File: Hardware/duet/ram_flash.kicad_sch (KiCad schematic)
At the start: 1 part, among them U2 W956D8MBYA5I

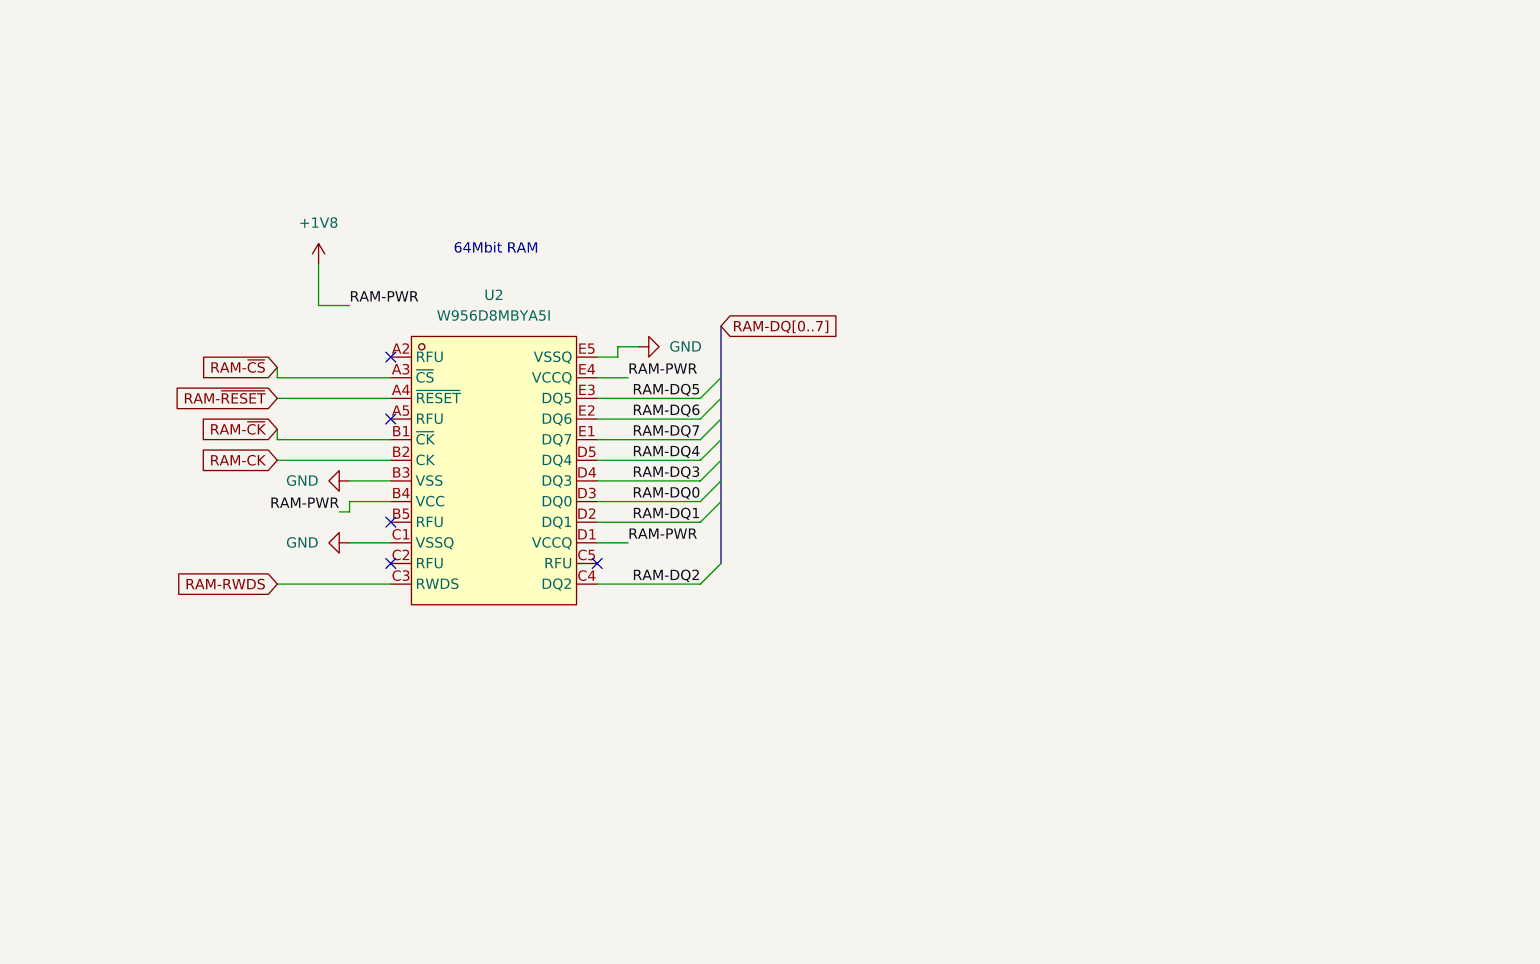
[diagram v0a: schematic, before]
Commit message: Add ECP5 configuration pins and labels
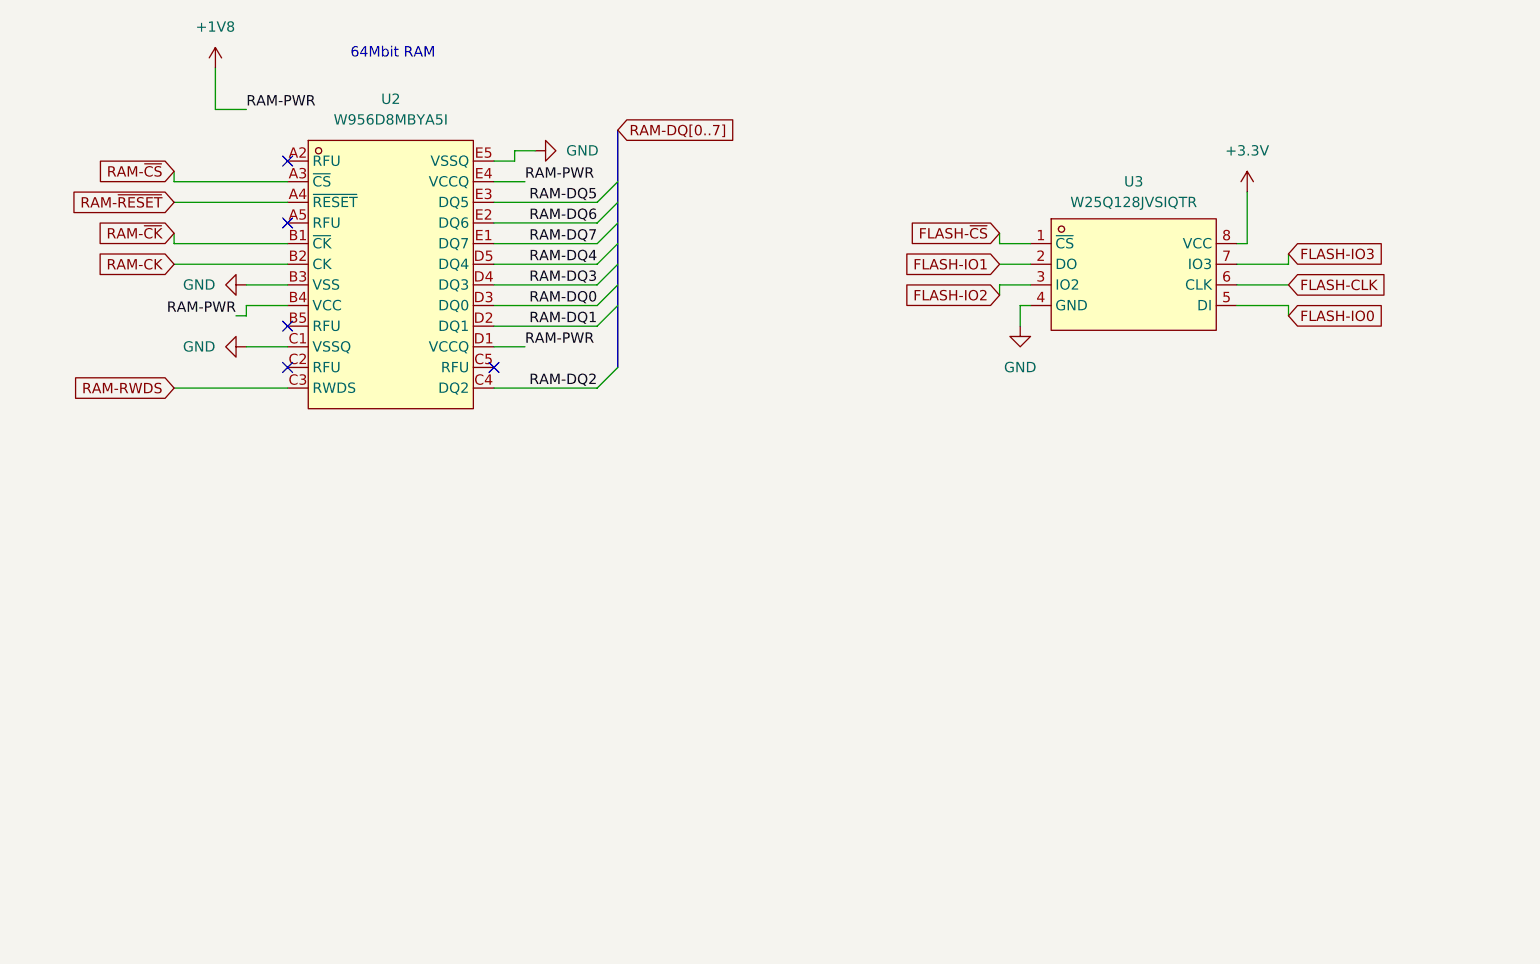
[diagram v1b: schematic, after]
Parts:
- added U3: W25Q128JVSIQTR, easyeda2kicad:SOIC-8_L5.3-W5.3-P1.27-LS8.0-BL, symbol easyeda2kicad:W25Q128JVSIQTR
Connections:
- net GND: now also U3.4 (GND)
- new net +3.3V: U3.8 (VCC)
- new net FLASH-CLK: U3.6 (CLK)
- new net FLASH-IO0: U3.5 (DI)
- new net FLASH-IO1: U3.2 (DO)
- new net FLASH-IO2: U3.3 (IO2)
- new net FLASH-IO3: U3.7 (IO3)
- new net FLASH-~{CS}: U3.1 (~{CS})
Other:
- moved on the sheet: U2

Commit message: Adds HDMI transmitter and connector
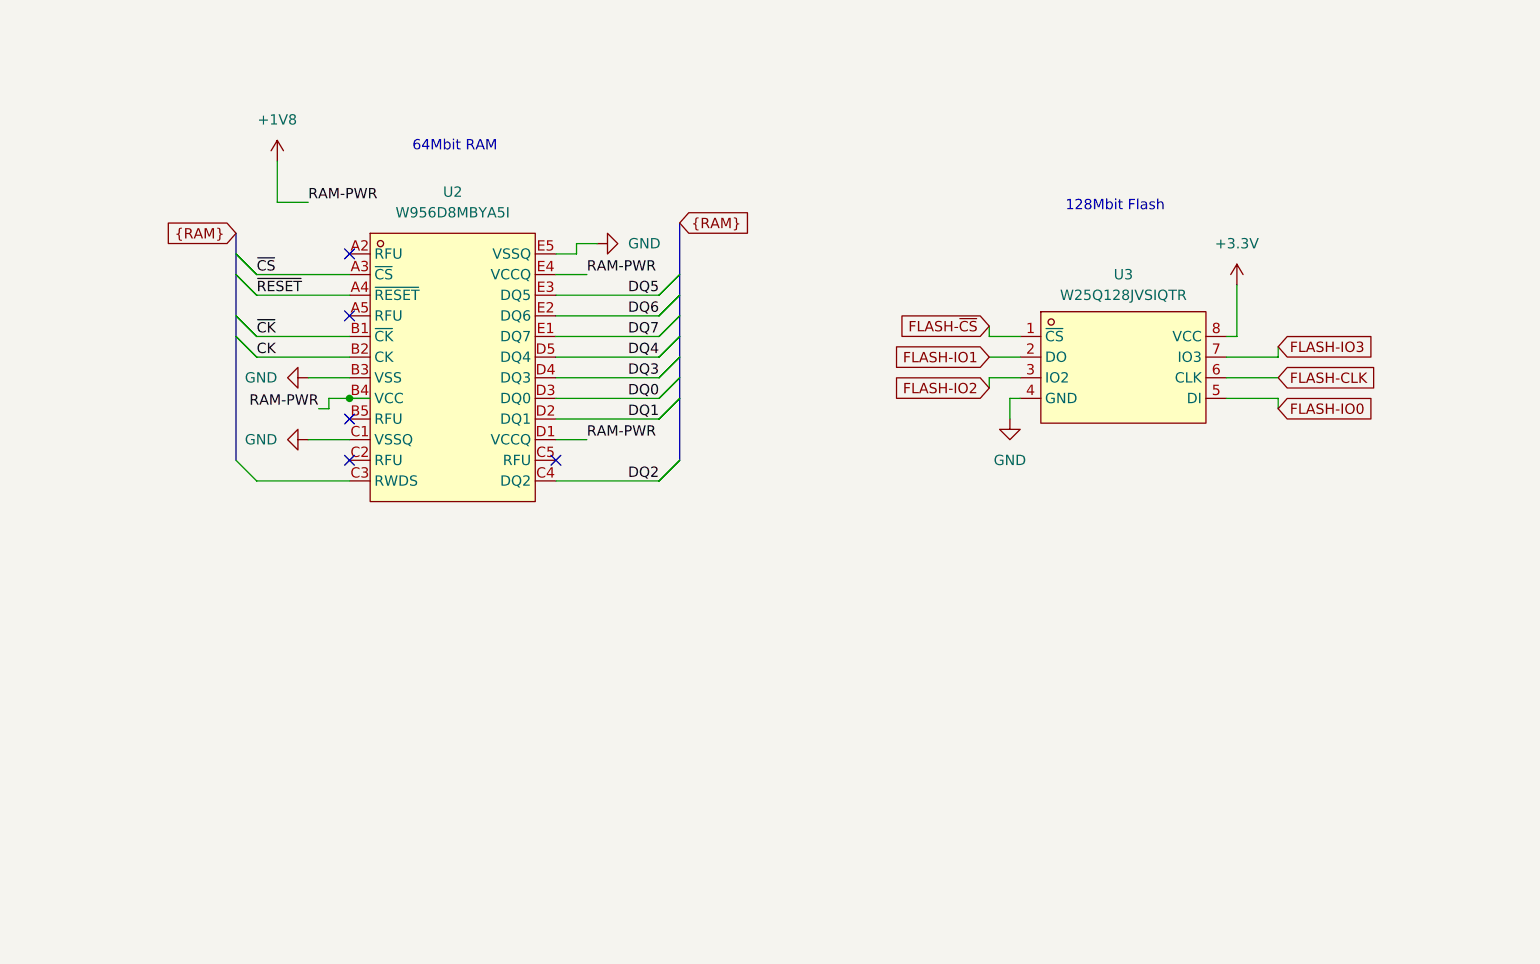
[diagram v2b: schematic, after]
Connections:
- net RAM-CK renamed CK
- net RAM-DQ0 renamed DQ0
- net RAM-DQ1 renamed DQ1
- net RAM-DQ2 renamed DQ2
- net RAM-DQ3 renamed DQ3
- net RAM-DQ4 renamed DQ4
- net RAM-DQ5 renamed DQ5
- net RAM-DQ6 renamed DQ6
- net RAM-DQ7 renamed DQ7
- net RAM-RWDS: no longer names the net of U2.C3 (RWDS)
- net RAM-~{CK} renamed ~{CK}
- net RAM-~{CS} renamed ~{CS}
- net RAM-~{RESET} renamed ~{RESET}
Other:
- note added: "128Mbit Flash"
- moved on the sheet: U2, U3

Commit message: Adds ESP32 and pull up-down resistors
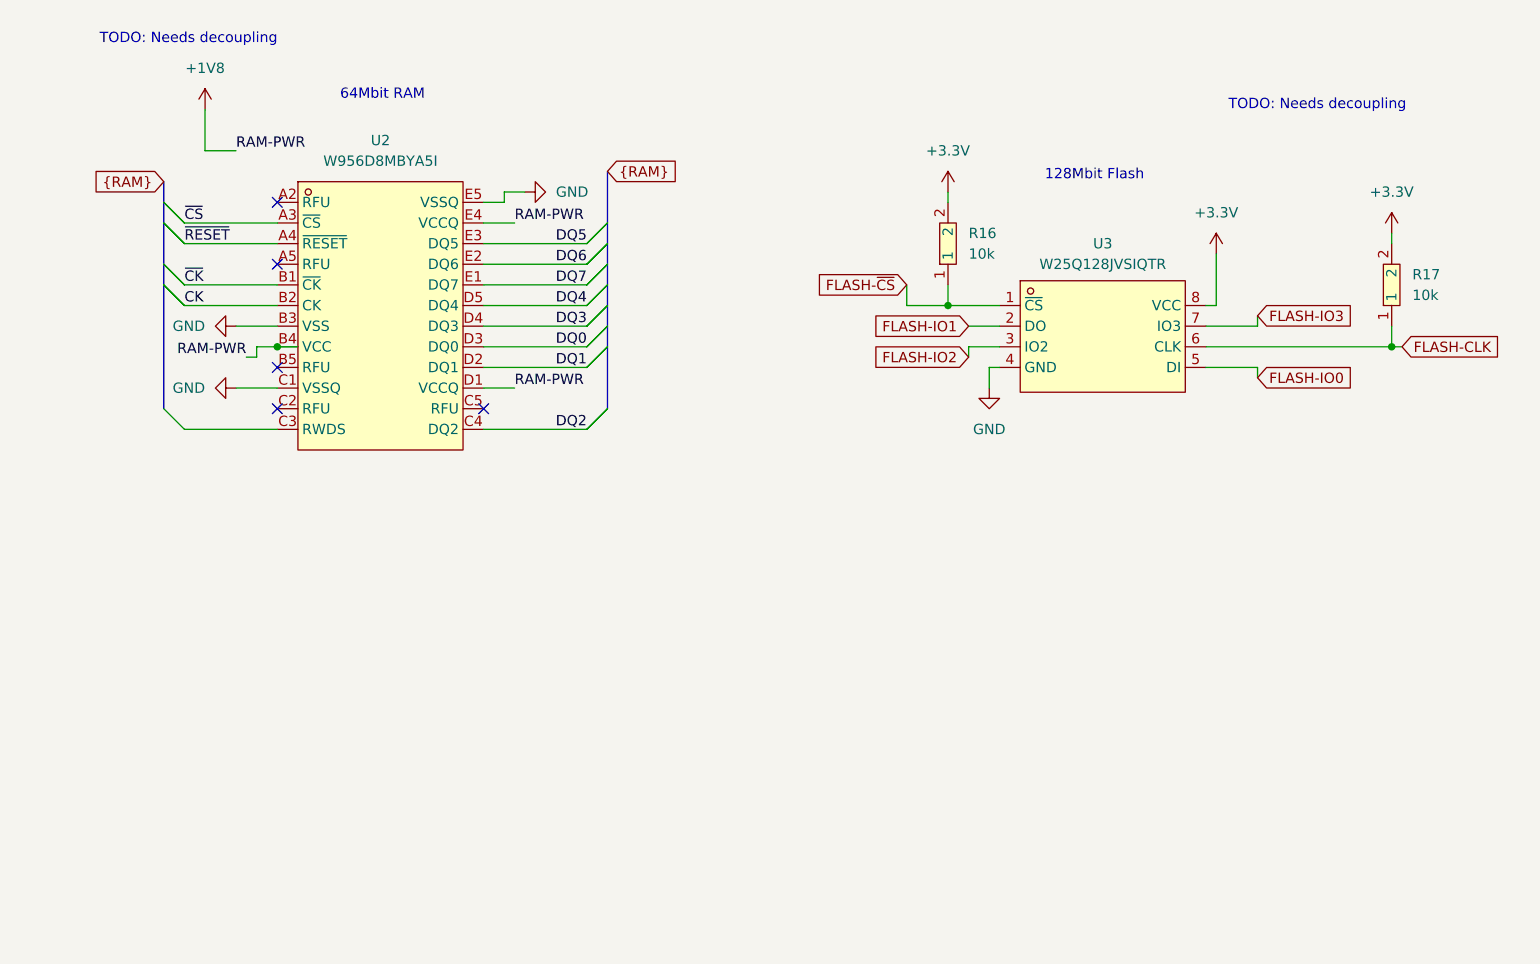
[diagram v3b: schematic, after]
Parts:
- added R16, R17: 10k, easyeda2kicad:R0402, symbol easyeda2kicad:0402WGF1002TCE
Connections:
- net +3.3V: now also R16.2, R17.2
- net FLASH-CLK: now also R17.1
- net FLASH-~{CS}: now also R16.1
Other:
- note added: "TODO: Needs decoupling"
- moved on the sheet: U2, U3

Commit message: Add mezzanine connector and finalze HDMI
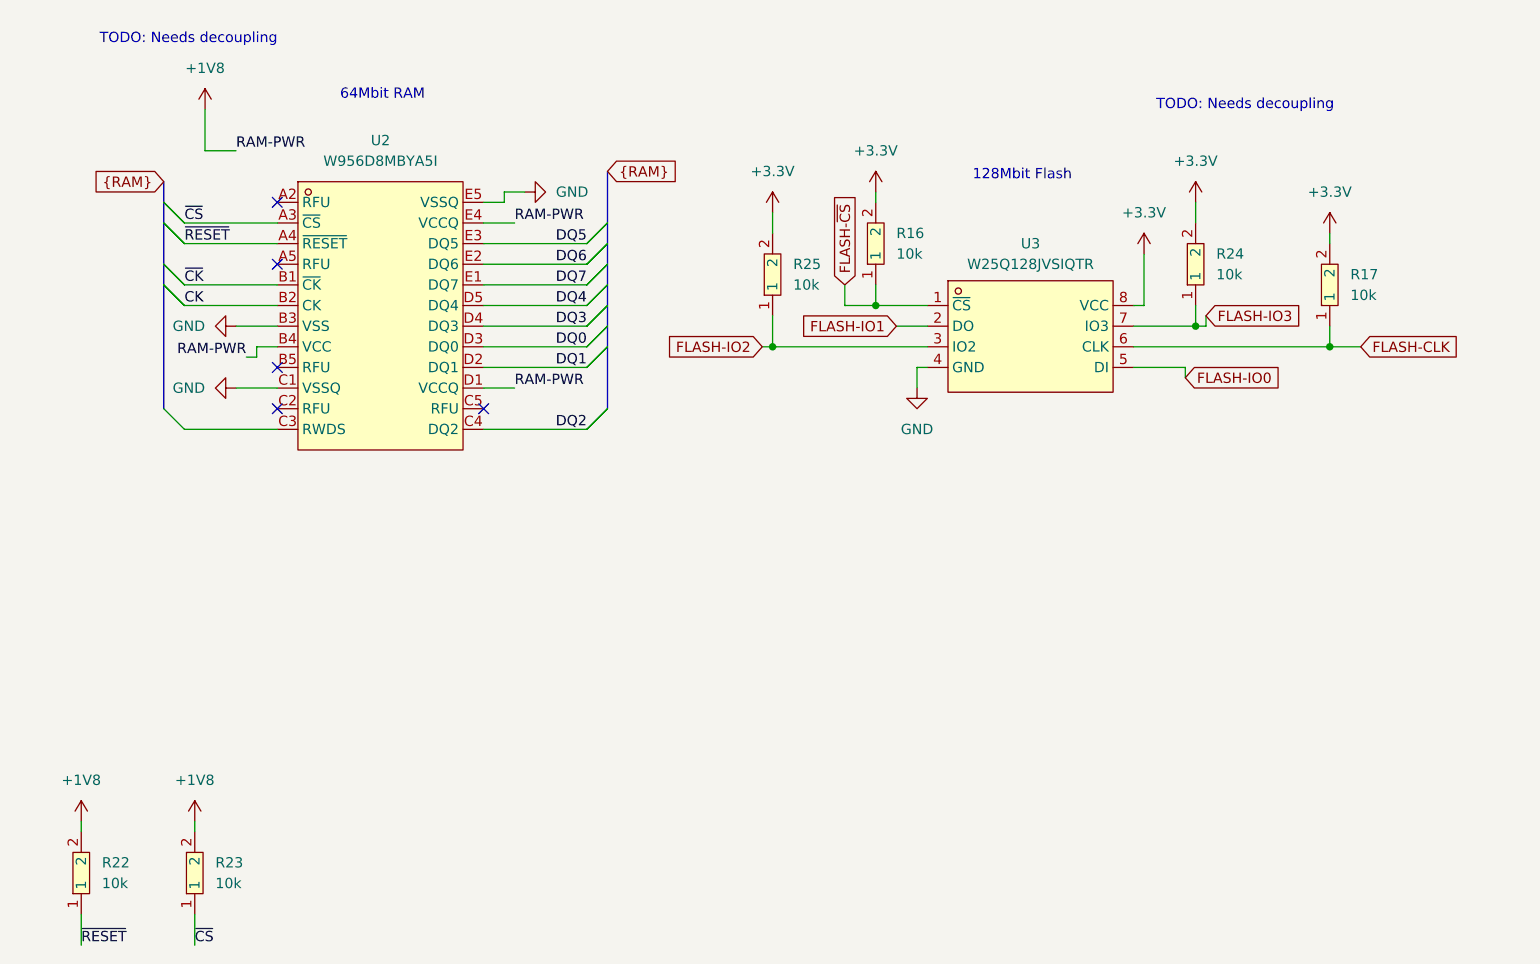
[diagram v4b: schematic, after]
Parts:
- added R22, R23, R24, R25: 10k, easyeda2kicad:R0402, symbol easyeda2kicad:0402WGF1002TCE
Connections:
- net +1V8: now also R22.2, R23.2
- net +3.3V: now also R24.2, R25.2
- net FLASH-IO2: now also R25.1
- net FLASH-IO3: now also R24.1
- net ~{CS}: now also R23.1
- net ~{RESET}: now also R22.1
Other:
- moved on the sheet: R16, R17, U3
